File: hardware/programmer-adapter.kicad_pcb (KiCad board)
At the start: 2 copper layers, 14.1 x 25.7 mm, 3 parts, among them J1 Power, J2 Target, J3 Conn_ARM_JTAG_SWD_20

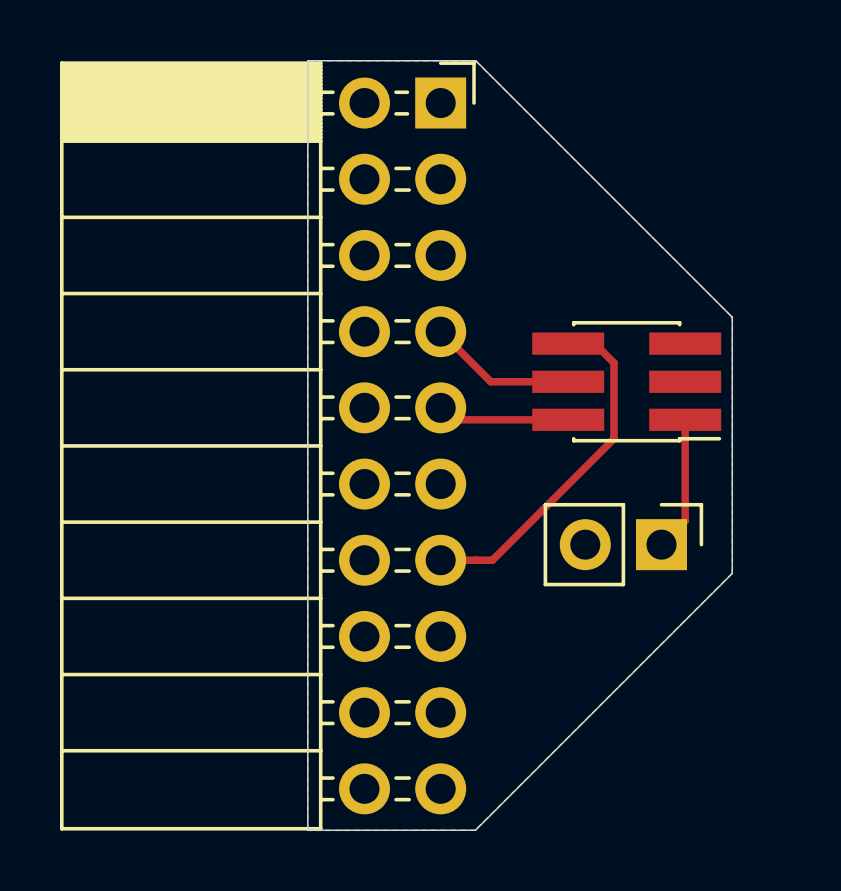
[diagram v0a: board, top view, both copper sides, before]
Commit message: Added power designators
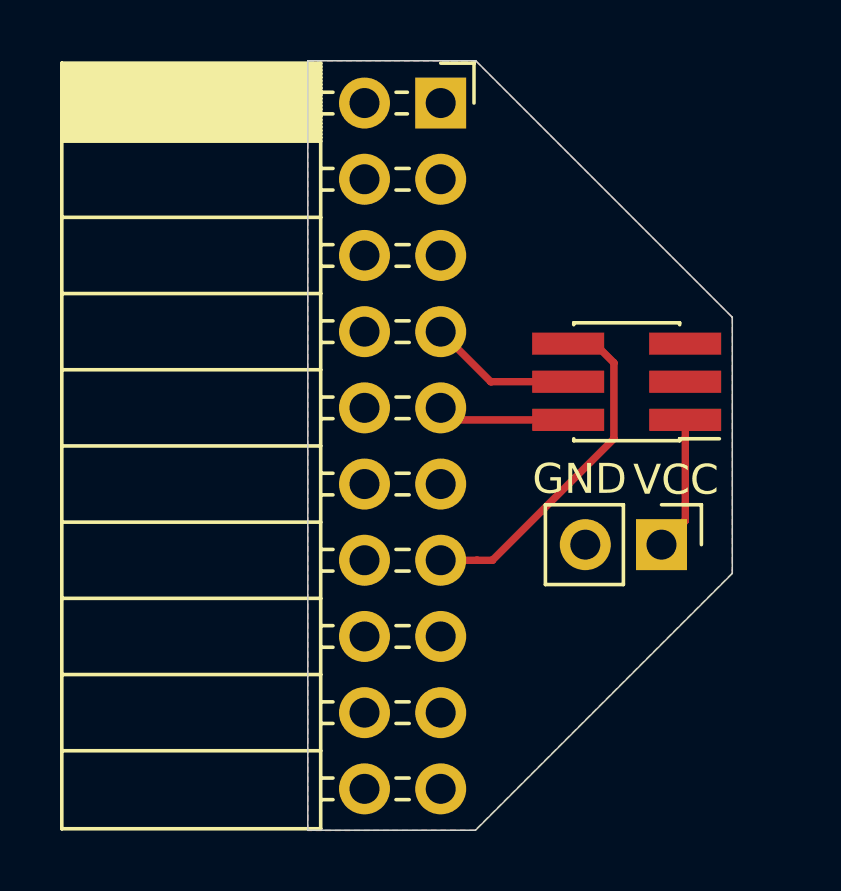
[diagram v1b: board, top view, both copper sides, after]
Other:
- board text added: "GND"
- board text added: "Programmer Adapter v1.0.1"
- board text added: "VCC"
- board text removed: "Programmer Adapter v1.0.0"
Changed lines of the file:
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@@
   (general
     (thickness 1.6)
-    (drawings 8)
+    (drawings 10)
     (tracks 12)
     (zones 0)
@@
   )
   (page A4)
+  (title_block
+    (title "Programmer adapter")
+    (date 2020-02-22)
+    (rev 1.0.1)
+  )
   (layers
     (0 F.Cu signal)
@@
     )
   )
-  (gr_text "Programmer Adapter\nv1.0.0" (at 144.77 98.09 90) (layer B.SilkS)
+  (gr_text GND (at 146.61 99.3) (layer F.SilkS)
+    (effects (font (size 1 1) (thickness 0.15)))
+  )
+  (gr_text VCC (at 149.82 99.33) (layer F.SilkS)
+    (effects (font (size 1 1) (thickness 0.15)))
+  )
+  (gr_text "Programmer Adapter\nv1.0.1" (at 144.77 98.09 90) (layer B.SilkS)
     (effects (font (size 1 1) (thickness 0.15)) (justify mirror))
   )

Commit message: Added reset signal
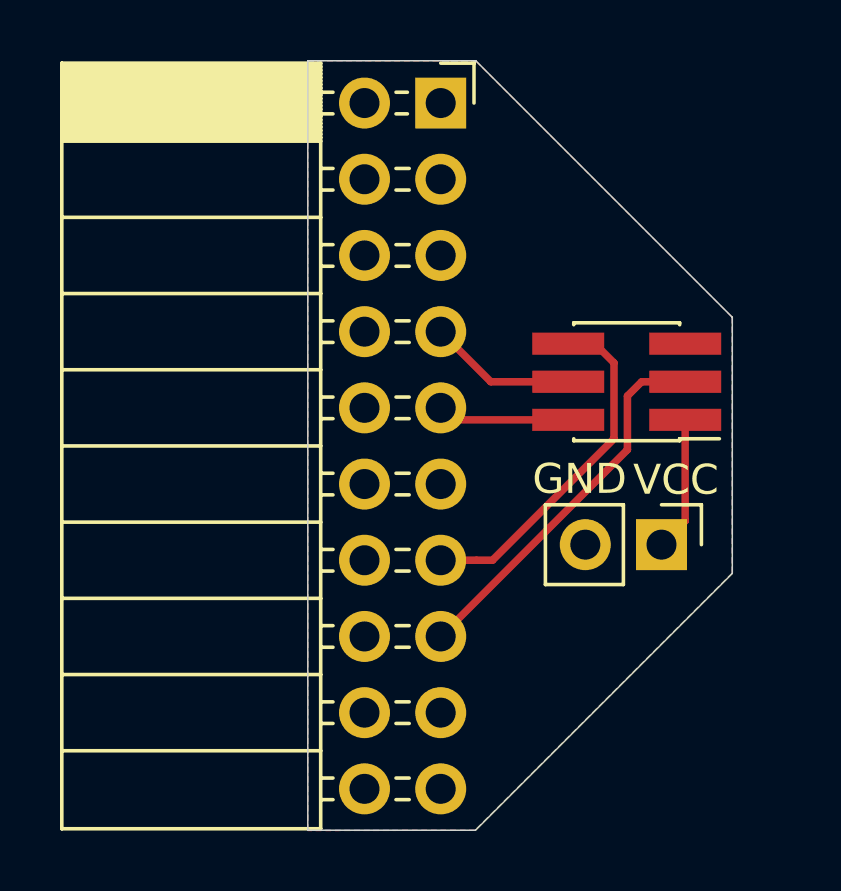
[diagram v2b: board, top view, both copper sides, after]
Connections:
- J2 pad 3: Net-(J2-Pad3) -> /reset
- J3 pad 15: Net-(J3-Pad15) -> /reset
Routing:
- net /reset: track 0.00 -> 12.7 mm
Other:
- board text added: "Programmer Adapter v1.1.0"
- board text removed: "Programmer Adapter v1.0.1"
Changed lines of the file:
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@@
     (thickness 1.6)
     (drawings 10)
-    (tracks 12)
+    (tracks 16)
     (zones 0)
     (modules 3)
-    (nets 14)
+    (nets 13)
   )
   (page A4)
   (title_block
     (title "Programmer adapter")
-    (date 2020-02-22)
-    (rev 1.0.1)
+    (date 2020-03-09)
+    (rev 1.1.0)
   )
   (layers
@@
   (net 3 /SWO)
   (net 4 /SWDIO)
-  (net 5 "Net-(J2-Pad3)")
-  (net 6 /SWDCLK)
-  (net 7 "Net-(J3-Pad19)")
-  (net 8 "Net-(J3-Pad17)")
-  (net 9 "Net-(J3-Pad15)")
-  (net 10 "Net-(J3-Pad11)")
-  (net 11 "Net-(J3-Pad5)")
-  (net 12 "Net-(J3-Pad3)")
-  (net 13 "Net-(J3-Pad2)")
+  (net 5 /SWDCLK)
+  (net 6 "Net-(J3-Pad19)")
+  (net 7 "Net-(J3-Pad17)")
+  (net 8 "Net-(J3-Pad11)")
+  (net 9 "Net-(J3-Pad5)")
+  (net 10 "Net-(J3-Pad3)")
+  (net 11 "Net-(J3-Pad2)")
+  (net 12 /reset)
   (net_class Default "This is the default net class."
     (clearance 0.2)
@@
     (add_net /SWDIO)
     (add_net /SWO)
+    (add_net /reset)
     (add_net GND)
-    (add_net "Net-(J2-Pad3)")
     (add_net "Net-(J3-Pad11)")
-    (add_net "Net-(J3-Pad15)")
     (add_net "Net-(J3-Pad17)")
     (add_net "Net-(J3-Pad19)")
@@
       (net 1 GND))
     (pad 19 thru_hole oval (at 0 22.86) (size 1.7 1.7) (drill 1) (layers *.Cu *.Mask)
-      (net 7 "Net-(J3-Pad19)"))
+      (net 6 "Net-(J3-Pad19)"))
     (pad 18 thru_hole oval (at -2.54 20.32) (size 1.7 1.7) (drill 1) (layers *.Cu *.Mask)
       (net 1 GND))
     (pad 17 thru_hole oval (at 0 20.32) (size 1.7 1.7) (drill 1) (layers *.Cu *.Mask)
-      (net 8 "Net-(J3-Pad17)"))
+      (net 7 "Net-(J3-Pad17)"))
     (pad 16 thru_hole oval (at -2.54 17.78) (size 1.7 1.7) (drill 1) (layers *.Cu *.Mask)
       (net 1 GND))
     (pad 15 thru_hole oval (at 0 17.78) (size 1.7 1.7) (drill 1) (layers *.Cu *.Mask)
-      (net 9 "Net-(J3-Pad15)"))
+      (net 12 /reset))
     (pad 14 thru_hole oval (at -2.54 15.24) (size 1.7 1.7) (drill 1) (layers *.Cu *.Mask)
       (net 1 GND))
@@
       (net 1 GND))
     (pad 11 thru_hole oval (at 0 12.7) (size 1.7 1.7) (drill 1) (layers *.Cu *.Mask)
-      (net 10 "Net-(J3-Pad11)"))
+      (net 8 "Net-(J3-Pad11)"))
     (pad 10 thru_hole oval (at -2.54 10.16) (size 1.7 1.7) (drill 1) (layers *.Cu *.Mask)
       (net 1 GND))
     (pad 9 thru_hole oval (at 0 10.16) (size 1.7 1.7) (drill 1) (layers *.Cu *.Mask)
-      (net 6 /SWDCLK))
+      (net 5 /SWDCLK))
     (pad 8 thru_hole oval (at -2.54 7.62) (size 1.7 1.7) (drill 1) (layers *.Cu *.Mask)
       (net 1 GND))
@@
       (net 1 GND))
     (pad 5 thru_hole oval (at 0 5.08) (size 1.7 1.7) (drill 1) (layers *.Cu *.Mask)
-      (net 11 "Net-(J3-Pad5)"))
+      (net 9 "Net-(J3-Pad5)"))
     (pad 4 thru_hole oval (at -2.54 2.54) (size 1.7 1.7) (drill 1) (layers *.Cu *.Mask)
       (net 1 GND))
     (pad 3 thru_hole oval (at 0 2.54) (size 1.7 1.7) (drill 1) (layers *.Cu *.Mask)
-      (net 12 "Net-(J3-Pad3)"))
+      (net 10 "Net-(J3-Pad3)"))
     (pad 2 thru_hole oval (at -2.54 0) (size 1.7 1.7) (drill 1) (layers *.Cu *.Mask)
-      (net 13 "Net-(J3-Pad2)"))
+      (net 11 "Net-(J3-Pad2)"))
     (pad 1 thru_hole rect (at 0 0) (size 1.7 1.7) (drill 1) (layers *.Cu *.Mask)
       (net 2 +3V3))
@@
       (net 4 /SWDIO))
     (pad 3 smd rect (at -1.95 0 180) (size 2.4 0.74) (layers F.Cu F.Paste F.Mask)
-      (net 5 "Net-(J2-Pad3)"))
+      (net 12 /reset))
     (pad 2 smd rect (at 1.95 -1.27 180) (size 2.4 0.74) (layers F.Cu F.Paste F.Mask)
-      (net 6 /SWDCLK))
+      (net 5 /SWDCLK))
     (pad 1 smd rect (at -1.95 -1.27 180) (size 2.4 0.74) (layers F.Cu F.Paste F.Mask)
       (net 2 +3V3))
@@
     (effects (font (size 1 1) (thickness 0.15)))
   )
-  (gr_text "Programmer Adapter\nv1.0.1" (at 144.77 98.09 90) (layer B.SilkS)
+  (gr_text "Programmer Adapter\nv1.1.0" (at 144.77 98.09 90) (layer B.SilkS)
     (effects (font (size 1 1) (thickness 0.15)) (justify mirror))
   )
@@
   (segment (start 143.65 96.06) (end 141.98 94.39) (width 0.25) (layer F.Cu) (net 4))
   (segment (start 146.23 96.06) (end 143.65 96.06) (width 0.25) (layer F.Cu) (net 4))
-  (segment (start 142.38 97.33) (end 141.98 96.93) (width 0.25) (layer F.Cu) (net 6))
-  (segment (start 146.23 97.33) (end 142.38 97.33) (width 0.25) (layer F.Cu) (net 6))
+  (segment (start 142.38 97.33) (end 141.98 96.93) (width 0.25) (layer F.Cu) (net 5))
+  (segment (start 146.23 97.33) (end 142.38 97.33) (width 0.25) (layer F.Cu) (net 5))
+  (segment (start 148.68 96.06) (end 150.13 96.06) (width 0.25) (layer F.Cu) (net 12))
+  (segment (start 148.205011 96.534989) (end 148.68 96.06) (width 0.25) (layer F.Cu) (net 12))
+  (segment (start 141.98 104.55) (end 148.205011 98.324989) (width 0.25) (layer F.Cu) (net 12))
+  (segment (start 148.205011 98.324989) (end 148.205011 96.534989) (width 0.25) (layer F.Cu) (net 12))
   (zone (net 1) (net_name GND) (layer F.Cu) (hatch edge 0.508)
     (connect_pads (clearance 0.127))

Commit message: Voltage Regulator Supply
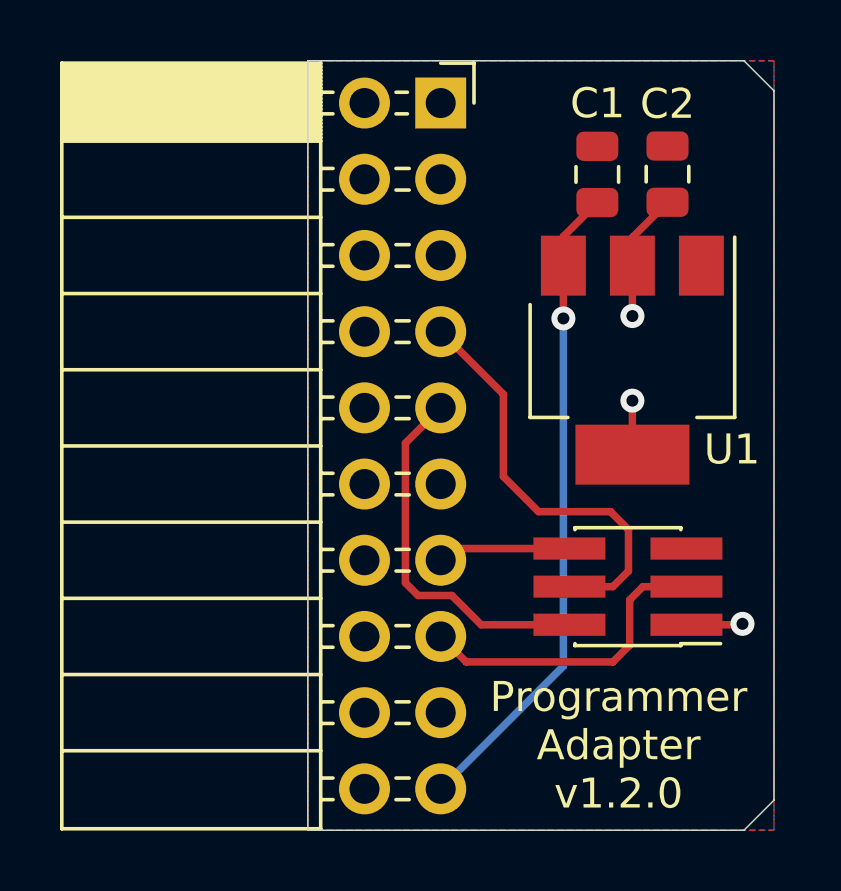
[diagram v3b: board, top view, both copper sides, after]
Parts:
- removed J1: Power, Connector_PinHeader_2.54mm:PinHeader_1x02_P2.54mm_Vertical
- added C1: 10u, Capacitor_SMD:C_0805_2012Metric, F.Cu at (147.2, 89.2)
- added C2: 22u, Capacitor_SMD:C_0805_2012Metric, F.Cu at (149.5, 89.1)
- added U1: AMS1117-3.3, Package_TO_SOT_SMD:SOT-223-3_TabPin2, F.Cu at (148.4, 95.3)
- moved J2 6.83 mm to (148.2, 102.9)
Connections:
- J3 pad 19: Net-(J3-Pad19) -> +5V
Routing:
- net +5V: track 0.00 -> 21.7 mm, vias 0 -> 1
- net /SWDIO: track 4.94 -> 14.2 mm
- net /SWDCLK: track 4.42 -> 12.4 mm
- net /SWO: track 11.8 -> 4.45 mm
- net +3V3: track 4.49 -> 7.96 mm, vias 0 -> 3
- net /reset: track 12.7 -> 10.5 mm
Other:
- board size 14.1 x 25.7 mm -> 15.5 x 25.7 mm
- board text added: "Programmer Adapter v1.2.0"
- board text removed: "GND"
- board text removed: "Programmer Adapter v1.1.0"
- board text removed: "VCC"

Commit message: Changed LDO to MCP1826S
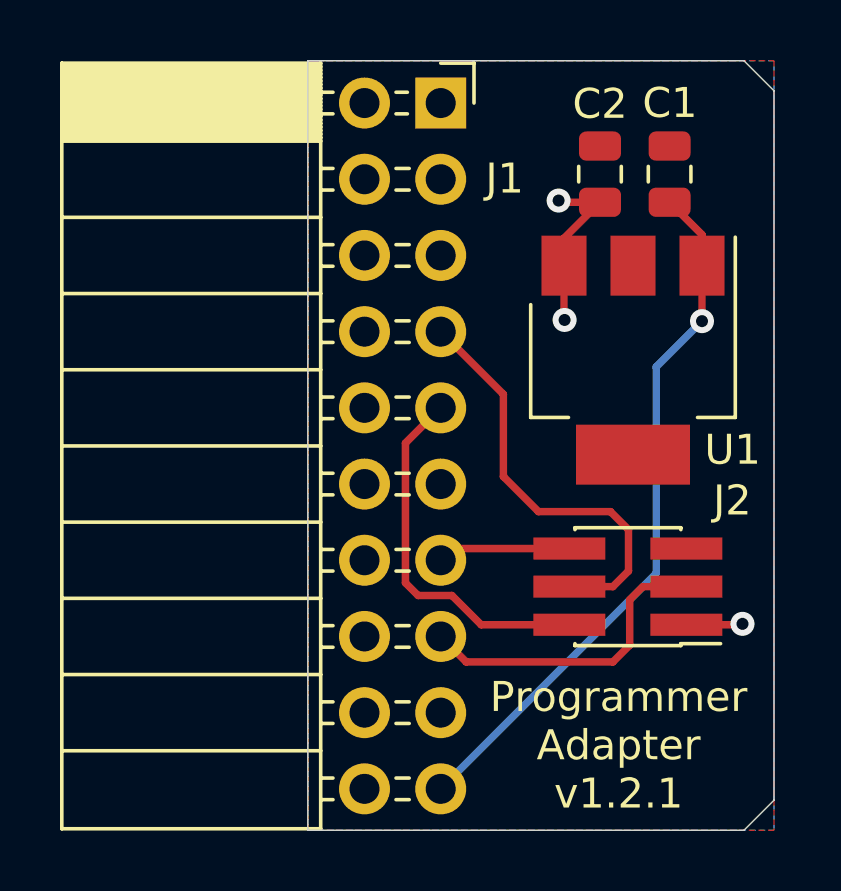
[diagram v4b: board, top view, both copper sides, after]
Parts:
- U1: value AMS1117-3.3 -> MCP1826S
- moved C1 2.41 mm to (149.6, 89.1)
- moved C2 2.25 mm to (147.3, 89.1)
- renumbered J3 to J1
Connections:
- U1 pad 1: GND -> +5V
- U1 pad 2: +3V3 -> GND
- U1 pad 3: +5V -> +3V3
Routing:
- net +5V: track 21.7 -> 23.6 mm
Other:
- board text added: "Programmer Adapter v1.2.1"
- board text removed: "Programmer Adapter v1.2.0"

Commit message: VCOM connection
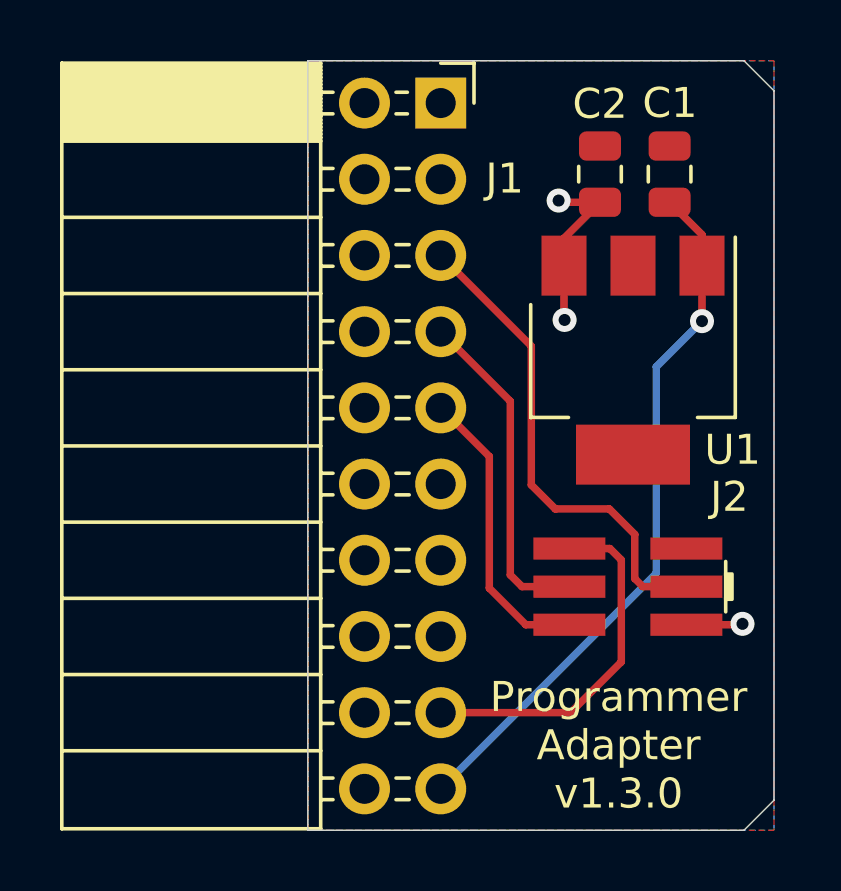
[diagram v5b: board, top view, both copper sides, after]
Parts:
- J2: value Target -> Conn_Chameleon_SWD; footprint Connector_PinHeader_1.27mm:PinHeader_2x03_P1.27mm_Vertical_SMD -> IoT_Home:Chameleon_SWD_Header
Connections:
- J1 pad 13: /SWO -> Net-(J1-Pad13)
- J1 pad 15: /reset -> Net-(J1-Pad15)
- J1 pad 17: Net-(J1-Pad17) -> /RX
- J1 pad 5: Net-(J1-Pad5) -> /TX
- J2 pad 3: /reset -> /TX
- J2 pad 6: /SWO -> /RX
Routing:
- net /TX: track 0.00 -> 16.3 mm
- net /RX: track 0.00 -> 12.0 mm
- net /reset: track 10.5 -> 0.00 mm
- net /SWO: track 4.45 -> 0.00 mm
- net /SWDCLK: track 12.4 -> 9.86 mm
- net /SWDIO: track 14.2 -> 12.1 mm
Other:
- board text added: "Programmer Adapter v1.3.0"
- board text removed: "Programmer Adapter v1.2.1"

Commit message: Fill zones
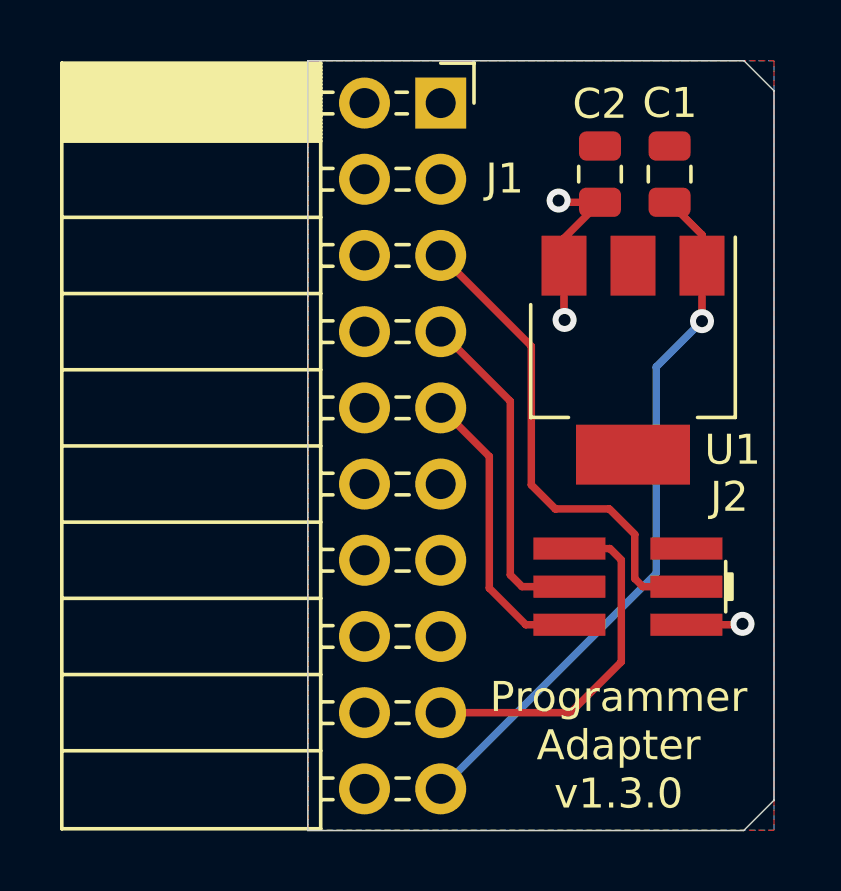
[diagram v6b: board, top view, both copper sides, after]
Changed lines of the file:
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@@
-      (effects (font (size 1 1) (thickness 0.15)))
-    )
-    (fp_text user %R (at 0 0 90) (layer F.Fab)
       (effects (font (size 1 1) (thickness 0.15)))
     )
@@
     (fp_line (start -3.26 -0.37) (end -3.26 -0.84) (layer F.SilkS) (width 0.12))
     (fp_poly (pts (xy -3.48 -0.43) (xy -3.25 -0.43) (xy -3.25 0.43) (xy -3.48 0.43)) (layer F.SilkS) (width 0.1))
+    (fp_text user %R (at 0 0 90) (layer F.Fab)
+      (effects (font (size 1 1) (thickness 0.15)))
+    )
     (pad 1 smd rect (at -1.95 -1.27 180) (size 2.4 0.74) (layers F.Cu F.Paste F.Mask)
       (net 2 +3V3))
@@
   )
   (gr_line (start 152.09 85.36) (end 153.09 86.36) (layer Edge.Cuts) (width 0.05))
-  (gr_line (start 152.09 111.01) (end 153.09 110.01) (layer Edge.Cuts) (width 0.05))
+  (gr_line (start 152.08 111.02) (end 153.09 110.01) (layer Edge.Cuts) (width 0.05))
   (gr_line (start 153.09 110.01) (end 153.09 86.36) (layer Edge.Cuts) (width 0.05))
   (gr_text "Programmer\nAdapter\nv1.3.0" (at 147.91 108.18) (layer F.SilkS)
     (effects (font (size 1 1) (thickness 0.15)))
   )
-  (gr_line (start 137.55 111.01) (end 152.09 111.01) (layer Edge.Cuts) (width 0.05))
-  (gr_line (start 137.55 85.36) (end 137.55 111.01) (layer Edge.Cuts) (width 0.05))
+  (gr_line (start 137.55 111.02) (end 152.08 111.02) (layer Edge.Cuts) (width 0.05))
+  (gr_line (start 137.55 85.36) (end 137.55 111.02) (layer Edge.Cuts) (width 0.05))
   (gr_line (start 137.55 85.36) (end 152.09 85.36) (layer Edge.Cuts) (width 0.05))
   (segment (start 152.01 104.16) (end 152.04 104.13) (width 0.25) (layer F.Cu) (net 2))

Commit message: Pending Changes
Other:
- rule pad_to_mask_clearance: 0.051 -> 0
